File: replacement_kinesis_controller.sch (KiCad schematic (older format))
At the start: 29 parts

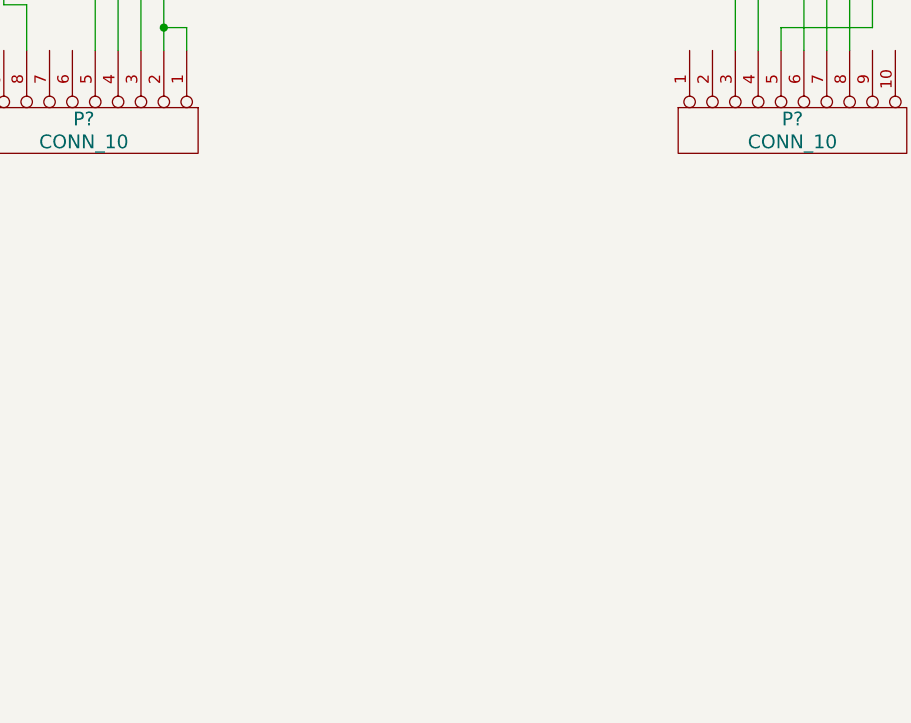
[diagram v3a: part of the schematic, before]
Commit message: Add IO expander
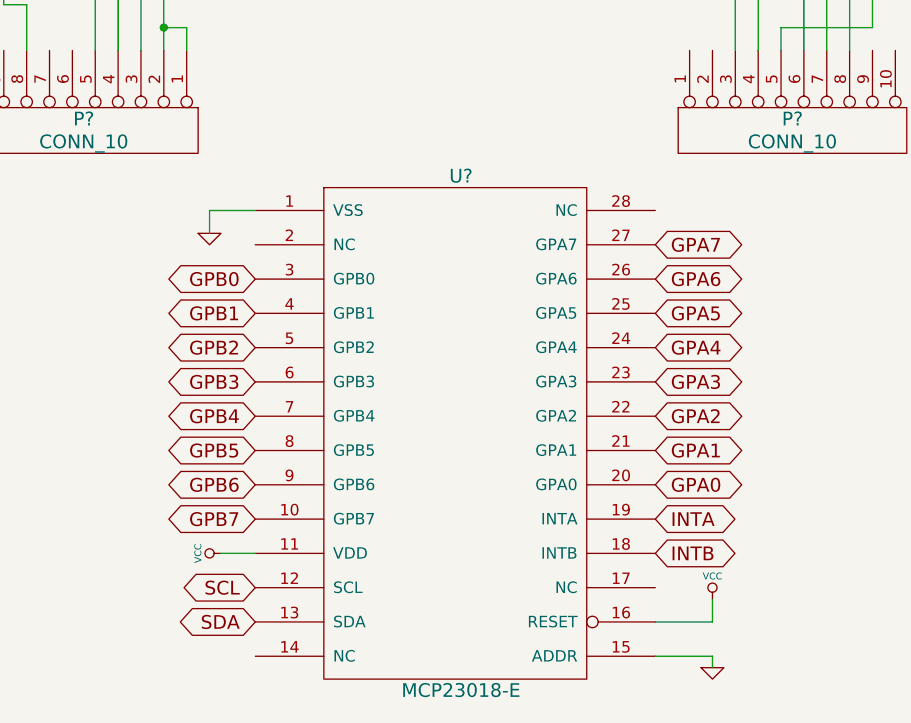
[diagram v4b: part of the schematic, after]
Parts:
- added U?: MCP23018-E, symbol MCP23018-E
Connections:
- net GND: now also U?.1 (VSS), U?.15 (ADDR)
- net VCC: now also U?.11 (VDD), U?.16 (RESET)
- new net GPA0: U?.20 (GPA0)
- new net GPA1: U?.21 (GPA1)
- new net GPA2: U?.22 (GPA2)
- new net GPA3: U?.23 (GPA3)
- new net GPA4: U?.24 (GPA4)
- new net GPA5: U?.25 (GPA5)
- new net GPA6: U?.26 (GPA6)
- new net GPA7: U?.27 (GPA7)
- new net GPB0: U?.3 (GPB0)
- new net GPB1: U?.4 (GPB1)
- new net GPB2: U?.5 (GPB2)
- new net GPB3: U?.6 (GPB3)
- new net GPB4: U?.7 (GPB4)
- new net GPB5: U?.8 (GPB5)
- new net GPB6: U?.9 (GPB6)
- new net GPB7: U?.10 (GPB7)
- new net INTA: U?.19 (INTA)
- new net INTB: U?.18 (INTB)
- new net SCL: U?.12 (SCL)
- new net SDA: U?.13 (SDA)
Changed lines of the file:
@@
 Text Label 7450 5600 0    60   ~ 0
 HWB
+$Comp
+L MCP23018-E U?
+U 1 1 54CAF2E5
+P 3300 6600
+F 0 "U?" H 3300 7700 60  0000 C CNN
+F 1 "MCP23018-E" H 3300 5450 60  0000 C CNN
+F 2 "" H 3300 6950 60  0000 C CNN
+F 3 "" H 3300 6950 60  0000 C CNN
+	1    3300 6600
+	1    0    0    -1
+$EndComp
+Text GLabel 4150 6850 2    60   BiDi ~ 0
+GPA0
+Text GLabel 4150 6700 2    60   BiDi ~ 0
+GPA1
+Text GLabel 4150 6550 2    60   BiDi ~ 0
+GPA2
+Text GLabel 4150 6400 2    60   BiDi ~ 0
+GPA3
+Text GLabel 4150 6250 2    60   BiDi ~ 0
+GPA4
+Text GLabel 4150 6100 2    60   BiDi ~ 0
+GPA5
+Text GLabel 4150 5950 2    60   BiDi ~ 0
+GPA6
+Text GLabel 4150 5800 2    60   BiDi ~ 0
+GPA7
+Text GLabel 2400 5950 0    60   BiDi ~ 0
+GPB0
+Text GLabel 2400 6100 0    60   BiDi ~ 0
+GPB1
+Text GLabel 2400 6250 0    60   BiDi ~ 0
+GPB2
+Text GLabel 2400 6400 0    60   BiDi ~ 0
+GPB3
+Text GLabel 2400 6550 0    60   BiDi ~ 0
+GPB4
+Text GLabel 2400 6700 0    60   BiDi ~ 0
+GPB5
+Text GLabel 2400 6850 0    60   BiDi ~ 0
+GPB6
+Text GLabel 2400 7000 0    60   BiDi ~ 0
+GPB7
+$Comp
+L GND #PWR?
+U 1 1 54CB370B
+P 2200 5750
+F 0 "#PWR?" H 2200 5750 30  0001 C CNN
+F 1 "GND" H 2200 5680 30  0001 C CNN
+F 2 "" H 2200 5750 60  0000 C CNN
+F 3 "" H 2200 5750 60  0000 C CNN
+	1    2200 5750
+	1    0    0    -1
+$EndComp
+Wire Wire Line
+	2400 5650 2200 5650
+Wire Wire Line
+	2200 5650 2200 5750
+$Comp
+L VCC #PWR?
+U 1 1 54CB597A
+P 2250 7150
+F 0 "#PWR?" H 2250 7250 30  0001 C CNN
+F 1 "VCC" H 2250 7250 30  0000 C CNN
+F 2 "" H 2250 7150 60  0000 C CNN
+F 3 "" H 2250 7150 60  0000 C CNN
+	1    2250 7150
+	0    -1   -1   0
+$EndComp
+Wire Wire Line
+	2400 7150 2250 7150
+$Comp
+L GND #PWR?
+U 1 1 54CB76C3
+P 4400 7650
+F 0 "#PWR?" H 4400 7650 30  0001 C CNN
+F 1 "GND" H 4400 7580 30  0001 C CNN
+F 2 "" H 4400 7650 60  0000 C CNN
+F 3 "" H 4400 7650 60  0000 C CNN
+	1    4400 7650
+	1    0    0    -1
+$EndComp
+$Comp
+L VCC #PWR?
+U 1 1 54CB7764
+P 4400 7350
+F 0 "#PWR?" H 4400 7450 30  0001 C CNN
+F 1 "VCC" H 4400 7450 30  0000 C CNN
+F 2 "" H 4400 7350 60  0000 C CNN
+F 3 "" H 4400 7350 60  0000 C CNN
+	1    4400 7350
+	1    0    0    -1
+$EndComp
+Wire Wire Line
+	4150 7450 4400 7450
+Wire Wire Line
+	4400 7450 4400 7350
+Wire Wire Line
+	4150 7600 4400 7600
+Wire Wire Line
+	4400 7600 4400 7650
+Text GLabel 2400 7300 0    60   BiDi ~ 0
+SCL
+Text GLabel 2400 7450 0    60   BiDi ~ 0
+SDA
+Text GLabel 4150 7000 2    60   BiDi ~ 0
+INTA
+Text GLabel 4150 7150 2    60   BiDi ~ 0
+INTB
 $EndSCHEMATC

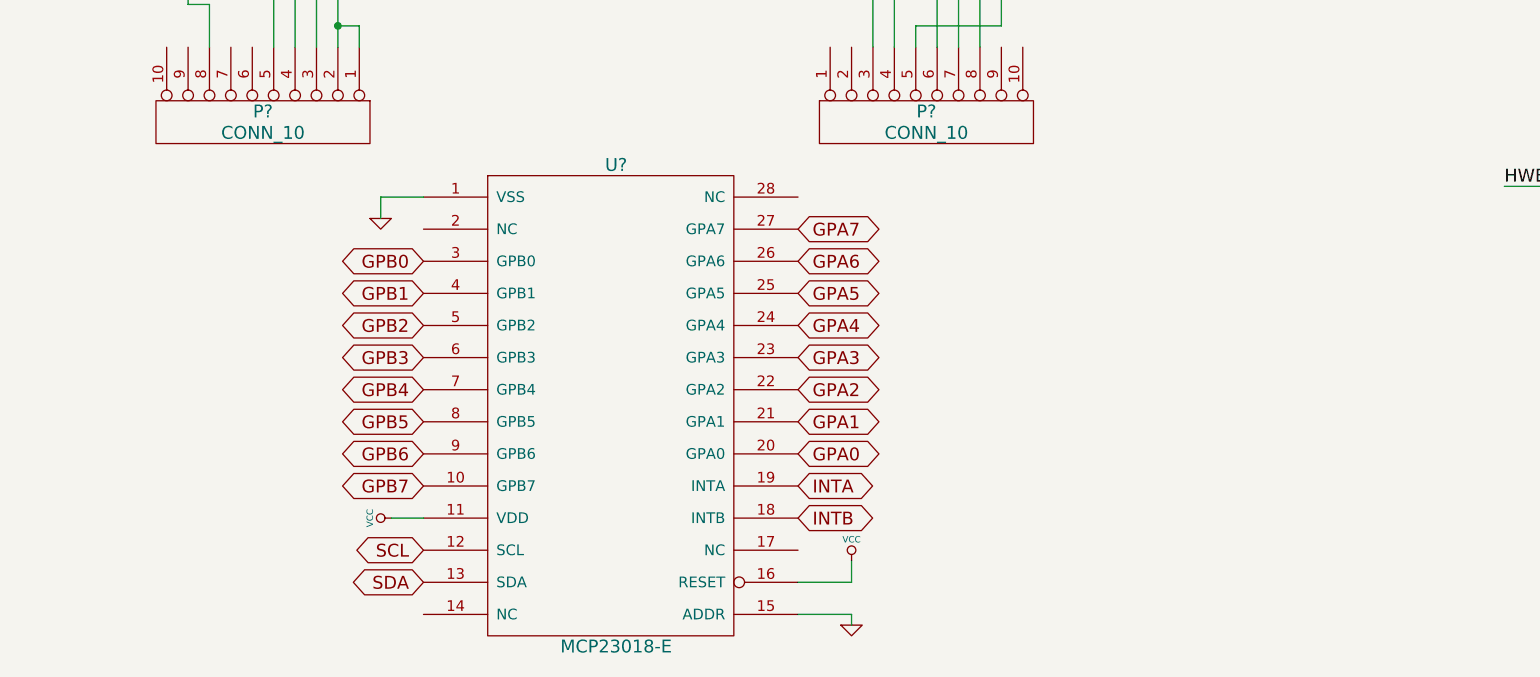
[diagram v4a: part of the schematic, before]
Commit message: Add matrix to IO map
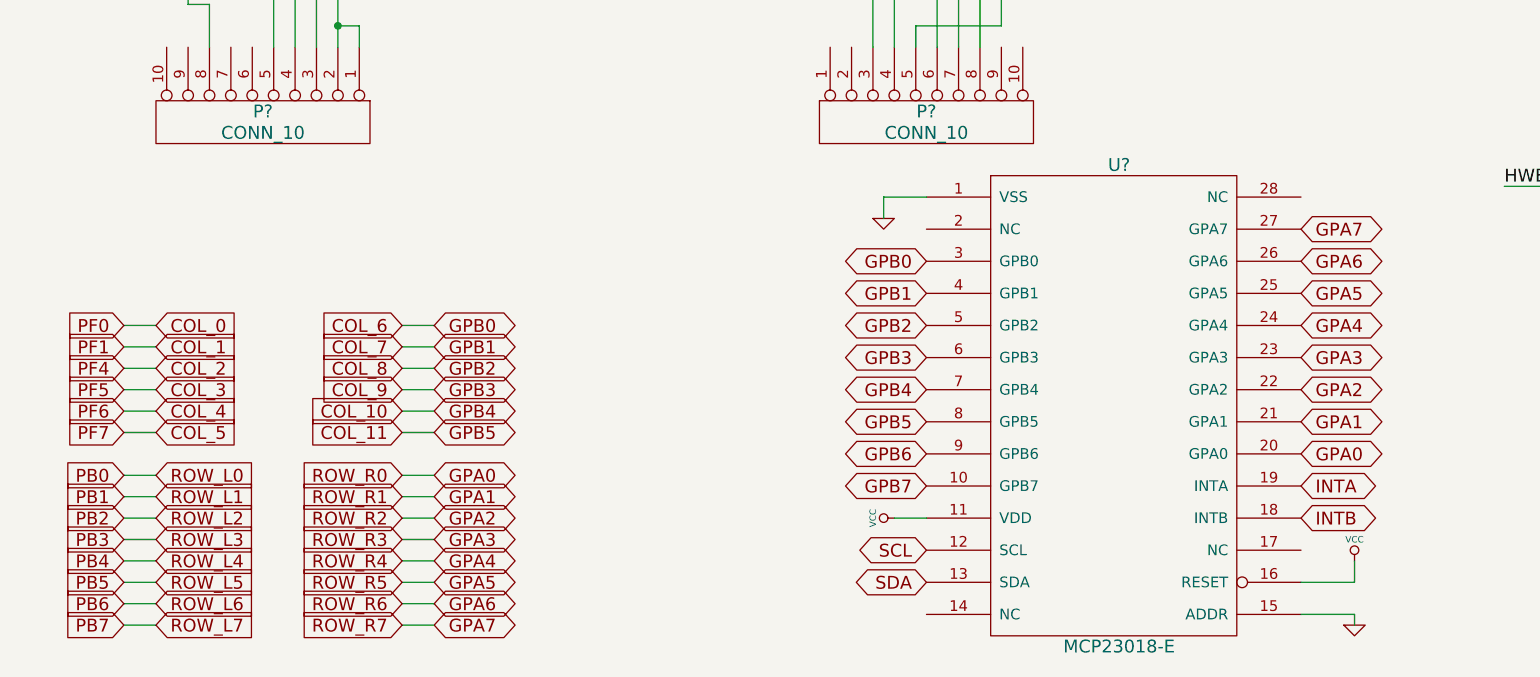
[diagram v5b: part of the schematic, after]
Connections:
- net GPB0 is gone; now on net COL_6: U?.3 (GPB0)
- net GPB1 is gone; now on net COL_7: U?.4 (GPB1)
- net GPB2 is gone; now on net COL_8: U?.5 (GPB2)
- net GPB3 is gone; now on net COL_9: U?.6 (GPB3)
- net GPB4 is gone; now on net COL_10: U?.7 (GPB4)
- net GPB5 is gone; now on net COL_11: U?.8 (GPB5)
- net PF0 is gone; now on net COL_0: P?.3 (P3), U?.41 ((ADC0)PF0)
- net PF1 is gone; now on net COL_1: P?.4 (P4), U?.40 ((ADC1)PF1)
- net PF4 is gone; now on net COL_2: P?.5 (P5), U?.39 ((ADC4/TCK)PF4)
- net PF5 is gone; now on net COL_3: P?.6 (P6), U?.38 ((ADC5/TMS)PF5)
- net PF6 is gone; now on net COL_4: P?.7 (P7), U?.37 ((ADC6/TDO)PF6)
- net PF7 is gone; now on net COL_5: P?.8 (P8), U?.36 ((ADC7/TDI)PF7)
- net ROW_L0 is gone; now on net PB0: P?.13 (P13)
- net ROW_L1 is gone; now on net PB1: P?.5 (P5)
- net ROW_L2 is gone; now on net PB2: P?.3 (P3)
- net ROW_L3 is gone; now on net PB3: P?.2 (P2)
- net ROW_L4 is gone; now on net PB4: P?.1 (P1)
- net ROW_L5 is gone; now on net PB5: P?.5 (P5)
- net ROW_L6 is gone; now on net PB6: P?.4 (P4), P?.8 (P8)
- net ROW_L7 is gone; now on net PB7: P?.1 (P1), P?.5 (P5)
- net ROW_R0 is gone; now on net GPA0: P?.10 (P10)
- net ROW_R1 is gone; now on net GPA1: P?.9 (P9)
- net ROW_R2 is gone; now on net GPA2: P?.8 (P8)
- net ROW_R3 is gone; now on net GPA3: P?.7 (P7)
- net ROW_R4 is gone; now on net GPA4: P?.4 (P4)
- net ROW_R5 is gone; now on net GPA5: P?.1 (P1), P?.6 (P6)
- net ROW_R6 is gone; now on net GPA6: P?.8 (P8), P?.9 (P9)
- net ROW_R7 is gone; now on net GPA7: P?.3 (P3), P?.4 (P4), P?.7 (P7)
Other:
- moved on the sheet: U?

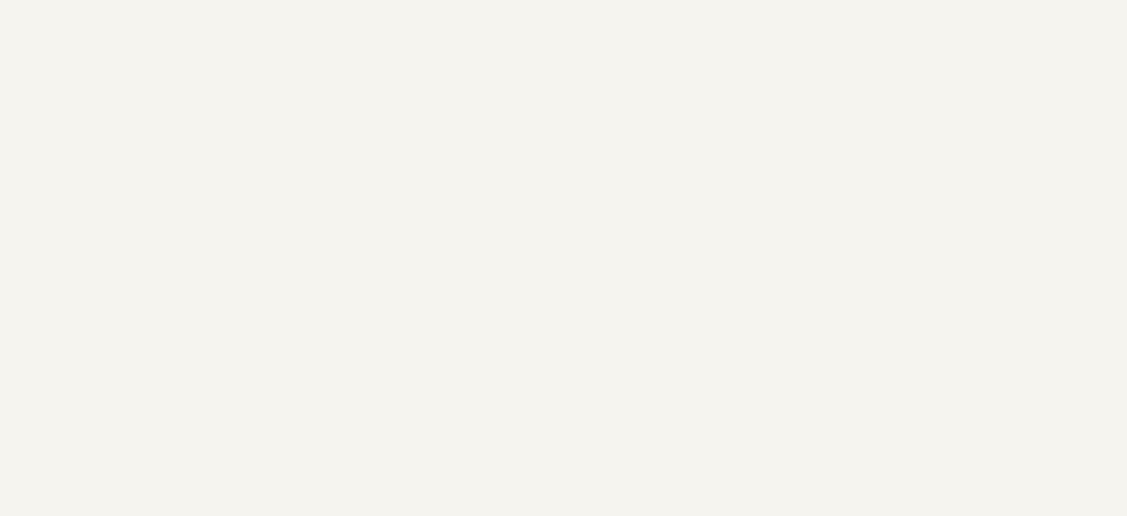
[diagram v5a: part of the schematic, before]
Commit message: Add lipo charging circuitry
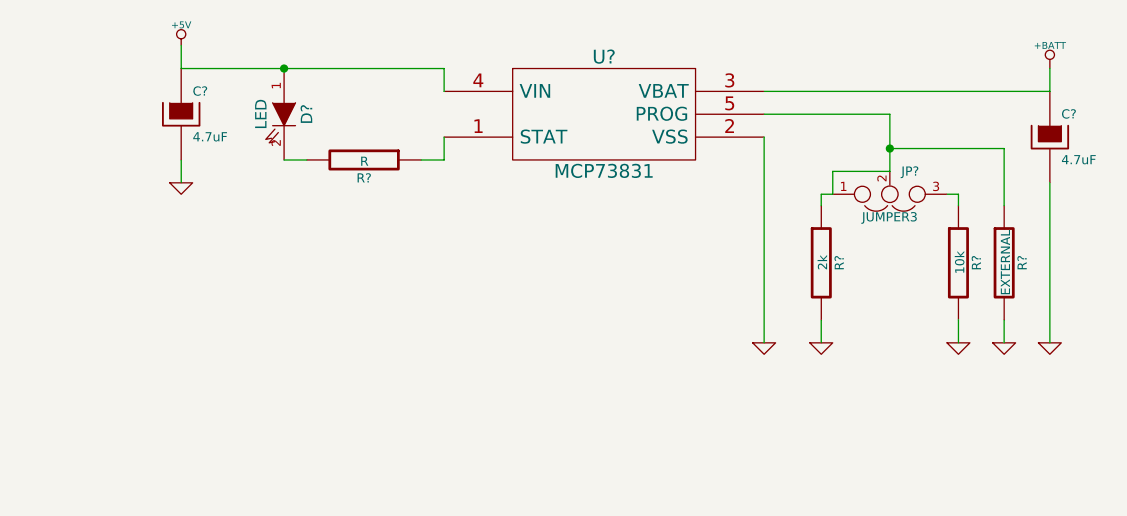
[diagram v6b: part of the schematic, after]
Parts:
- added C? (x2): 4.7uF, symbol CP
- added D?: LED, symbol LED
- added JP?: JUMPER3, symbol JUMPER3
- added R?: 2k, symbol R
- added R?: 10k, symbol R
- added R?: EXTERNAL, symbol R
- added R?: R, symbol R
- added U?: MCP73831, symbol MCP73831
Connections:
- net +5V: now also C?.1, D?.1 (A), U?.4 (VIN)
- net GND: now also C?.2, C?.2, R?.2, R?.2, R?.2, U?.2 (VSS)
- new net: D?.2 (K), R?.2
- new net: R?.1, U?.1 (STAT)
- new net: JP?.1, JP?.2, R?.1, R?.1, U?.5 (PROG)
- new net: JP?.3, R?.1
- new net +BATT: C?.1, U?.3 (VBAT)
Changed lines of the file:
@@
 Wire Wire Line
 	2450 6250 2300 6250
+$Comp
+L +5V #PWR?
+U 1 1 54CF080E
+P 7200 -1500
+F 0 "#PWR?" H 7200 -1410 20  0001 C CNN
+F 1 "+5V" H 7200 -1410 30  0000 C CNN
+F 2 "" H 7200 -1500 60  0000 C CNN
+F 3 "" H 7200 -1500 60  0000 C CNN
+	1    7200 -1500
+	1    0    0    -1
+$EndComp
+$Comp
+L GND #PWR?
+U 1 1 54CF0837
+P 7200 -900
+F 0 "#PWR?" H 7200 -900 30  0001 C CNN
+F 1 "GND" H 7200 -970 30  0001 C CNN
+F 2 "" H 7200 -900 60  0000 C CNN
+F 3 "" H 7200 -900 60  0000 C CNN
+	1    7200 -900
+	1    0    0    -1
+$EndComp
+$Comp
+L CP C?
+U 1 1 54CF089C
+P 7200 -1200
+F 0 "C?" H 7250 -1100 40  0000 L CNN
+F 1 "4.7uF" H 7250 -1300 40  0000 L CNN
+F 2 "" H 7300 -1350 30  0000 C CNN
+F 3 "" H 7200 -1200 300 0000 C CNN
+	1    7200 -1200
+	1    0    0    -1
+$EndComp
+$Comp
+L LED D?
+U 1 1 54CF0C60
+P 7650 -1200
+F 0 "D?" H 7650 -1100 50  0000 C CNN
+F 1 "LED" H 7650 -1300 50  0000 C CNN
+F 2 "" H 7650 -1200 60  0000 C CNN
+F 3 "" H 7650 -1200 60  0000 C CNN
+	1    7650 -1200
+	0    1    1    0
+$EndComp
+$Comp
+L MCP73831 U?
+U 1 1 54CF0F9B
+P 9050 -1250
+F 0 "U?" H 9050 -1050 60  0000 C CNN
+F 1 "MCP73831" H 9050 -1550 60  0000 C CNN
+F 2 "" H 9050 -1250 60  0000 C CNN
+F 3 "" H 9050 -1250 60  0000 C CNN
+	1    9050 -1250
+	1    0    0    -1
+$EndComp
+$Comp
+L JUMPER3 JP?
+U 1 1 54CF1C8F
+P 10300 -850
+F 0 "JP?" H 10350 -950 40  0000 L CNN
+F 1 "JUMPER3" H 10300 -750 40  0000 C CNN
+F 2 "" H 10300 -850 60  0000 C CNN
+F 3 "" H 10300 -850 60  0000 C CNN
+	1    10300 -850
+	1    0    0    1
+$EndComp
+$Comp
+L R R?
+U 1 1 54CF31F0
+P 10000 -550
+F 0 "R?" V 10080 -550 40  0000 C CNN
+F 1 "2k" V 10007 -549 40  0000 C CNN
+F 2 "" V 9930 -550 30  0000 C CNN
+F 3 "" H 10000 -550 30  0000 C CNN
+	1    10000 -550
+	1    0    0    -1
+$EndComp
+$Comp
+L R R?
+U 1 1 54CF4003
+P 10600 -550
+F 0 "R?" V 10680 -550 40  0000 C CNN
+F 1 "10k" V 10607 -549 40  0000 C CNN
+F 2 "" V 10530 -550 30  0000 C CNN
+F 3 "" H 10600 -550 30  0000 C CNN
+	1    10600 -550
+	1    0    0    -1
+$EndComp
+$Comp
+L R R?
+U 1 1 54CF404F
+P 10800 -550
+F 0 "R?" V 10880 -550 40  0000 C CNN
+F 1 "EXTERNAL" V 10807 -549 40  0000 C CNN
+F 2 "" V 10730 -550 30  0000 C CNN
+F 3 "" H 10800 -550 30  0000 C CNN
+	1    10800 -550
+	1    0    0    -1
+$EndComp
+$Comp
+L CP C?
+U 1 1 54CF4EE3
+P 11000 -1100
+F 0 "C?" H 11050 -1000 40  0000 L CNN
+F 1 "4.7uF" H 11050 -1200 40  0000 L CNN
+F 2 "" H 11100 -1250 30  0000 C CNN
+F 3 "" H 11000 -1100 300 0000 C CNN
+	1    11000 -1100
+	1    0    0    -1
+$EndComp
+Wire Wire Line
+	7200 -1500 7200 -1400
+Wire Wire Line
+	7200 -1400 8350 -1400
+Wire Wire Line
+	7200 -900 7200 -1000
+$Comp
+L R R?
+U 1 1 54CF9105
+P 8000 -1000
+F 0 "R?" V 8080 -1000 40  0000 C CNN
+F 1 "R" V 8007 -999 40  0000 C CNN
+F 2 "" V 7930 -1000 30  0000 C CNN
+F 3 "" H 8000 -1000 30  0000 C CNN
+	1    8000 -1000
+	0    1    1    0
+$EndComp
+Wire Wire Line
+	7650 -1000 7750 -1000
+Wire Wire Line
+	8250 -1000 8350 -1000
+Wire Wire Line
+	8350 -1000 8350 -1100
+Wire Wire Line
+	8350 -1400 8350 -1300
+Connection ~ 7650 -1400
+$Comp
+L GND #PWR?
+U 1 1 54CFC5E2
+P 9750 -200
+F 0 "#PWR?" H 9750 -200 30  0001 C CNN
+F 1 "GND" H 9750 -270 30  0001 C CNN
+F 2 "" H 9750 -200 60  0000 C CNN
+F 3 "" H 9750 -200 60  0000 C CNN
+	1    9750 -200
+	1    0    0    -1
+$EndComp
+$Comp
+L GND #PWR?
+U 1 1 54CFCA58
+P 10000 -200
+F 0 "#PWR?" H 10000 -200 30  0001 C CNN
+F 1 "GND" H 10000 -270 30  0001 C CNN
+F 2 "" H 10000 -200 60  0000 C CNN
+F 3 "" H 10000 -200 60  0000 C CNN
+	1    10000 -200
+	1    0    0    -1
+$EndComp
+$Comp
+L GND #PWR?
+U 1 1 54CFCA8A
+P 10600 -200
+F 0 "#PWR?" H 10600 -200 30  0001 C CNN
+F 1 "GND" H 10600 -270 30  0001 C CNN
+F 2 "" H 10600 -200 60  0000 C CNN
+F 3 "" H 10600 -200 60  0000 C CNN
+	1    10600 -200
+	1    0    0    -1
+$EndComp
+$Comp
+L GND #PWR?
+U 1 1 54CFCABC
+P 10800 -200
+F 0 "#PWR?" H 10800 -200 30  0001 C CNN
+F 1 "GND" H 10800 -270 30  0001 C CNN
+F 2 "" H 10800 -200 60  0000 C CNN
+F 3 "" H 10800 -200 60  0000 C CNN
+	1    10800 -200
+	1    0    0    -1
+$EndComp
+$Comp
+L GND #PWR?
+U 1 1 54CFCFCE
+P 11000 -200
+F 0 "#PWR?" H 11000 -200 30  0001 C CNN
+F 1 "GND" H 11000 -270 30  0001 C CNN
+F 2 "" H 11000 -200 60  0000 C CNN
+F 3 "" H 11000 -200 60  0000 C CNN
+	1    11000 -200
+	1    0    0    -1
+$EndComp
+Wire Wire Line
+	9750 -1100 9750 -200
+Wire Wire Line
+	10000 -200 10000 -300
+Wire Wire Line
+	10600 -200 10600 -300
+Wire Wire Line
+	10800 -200 10800 -300
+Wire Wire Line
+	11000 -200 11000 -900
+Wire Wire Line
+	9750 -1200 10300 -1200
+Wire Wire Line
+	10300 -1200 10300 -950
+Wire Wire Line
+	10050 -850 10000 -850
+Wire Wire Line
+	10000 -850 10000 -800
+Wire Wire Line
+	10550 -850 10600 -850
+Wire Wire Line
+	10600 -850 10600 -800
+Wire Wire Line
+	10800 -800 10800 -1050
+Wire Wire Line
+	10800 -1050 10300 -1050
+Connection ~ 10300 -1050
+Wire Wire Line
+	10300 -950 10050 -950
+Wire Wire Line
+	10050 -950 10050 -850
+Wire Wire Line
+	9750 -1300 11000 -1300
+Wire Wire Line
+	11000 -1300 11000 -1400
+$Comp
+L +BATT #PWR?
+U 1 1 54CFE044
+P 11000 -1400
+F 0 "#PWR?" H 11000 -1450 20  0001 C CNN
+F 1 "+BATT" H 11000 -1300 30  0000 C CNN
+F 2 "" H 11000 -1400 60  0000 C CNN
+F 3 "" H 11000 -1400 60  0000 C CNN
+	1    11000 -1400
+	1    0    0    -1
+$EndComp
 $EndSCHEMATC

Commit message: Add battery connector (should be JST connector)
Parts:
- added P?: CONN_2, symbol CONN_2
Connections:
- net +BATT: now also P?.1 (P1)
- net GND: now also P?.2 (PM)
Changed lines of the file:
@@
 	10050 -950 10050 -850
 Wire Wire Line
-	9750 -1300 11000 -1300
+	9750 -1300 11400 -1300
 Wire Wire Line
 	11000 -1300 11000 -1400
@@
 	1    0    0    -1
 $EndComp
+$Comp
+L CONN_2 P?
+U 1 1 54D026FC
+P 11750 -1200
+F 0 "P?" V 11700 -1200 40  0000 C CNN
+F 1 "CONN_2" V 11800 -1200 40  0000 C CNN
+F 2 "" H 11750 -1200 60  0000 C CNN
+F 3 "" H 11750 -1200 60  0000 C CNN
+	1    11750 -1200
+	1    0    0    -1
+$EndComp
+Connection ~ 11000 -1300
+$Comp
+L GND #PWR?
+U 1 1 54D028B7
+P 11400 -200
+F 0 "#PWR?" H 11400 -200 30  0001 C CNN
+F 1 "GND" H 11400 -270 30  0001 C CNN
+F 2 "" H 11400 -200 60  0000 C CNN
+F 3 "" H 11400 -200 60  0000 C CNN
+	1    11400 -200
+	1    0    0    -1
+$EndComp
+Wire Wire Line
+	11400 -1100 11400 -200
 $EndSCHEMATC

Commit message: Add WT12 symbol
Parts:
- added U?: WT12-A, symbol WT12-A
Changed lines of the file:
@@
 Wire Wire Line
 	11400 -1100 11400 -200
+$Comp
+L WT12-A U?
+U 1 1 54D0470D
+P 4450 -1300
+F 0 "U?" H 4100 -600 60  0000 C CNN
+F 1 "WT12-A" H 4450 -2200 60  0000 C CNN
+F 2 "" H 4450 -1100 60  0000 C CNN
+F 3 "" H 4450 -1100 60  0000 C CNN
+	1    4450 -1300
+	1    0    0    -1
+$EndComp
 $EndSCHEMATC
